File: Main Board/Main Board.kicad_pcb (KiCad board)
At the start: 4 copper layers, 100 x 62.5 mm, 104 parts, among them IC1 ESP32-S3-WROOM-1-N8R2, IC2 TPS65185RSLT, IC4 AP61100, J2 5023520300, J3 FH26W-39S-0.3SHW(60), J4 5023520500, J5 MSD-1-A, J6 5023520200, Q1 2N7002, Q2 BSS84-7-F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

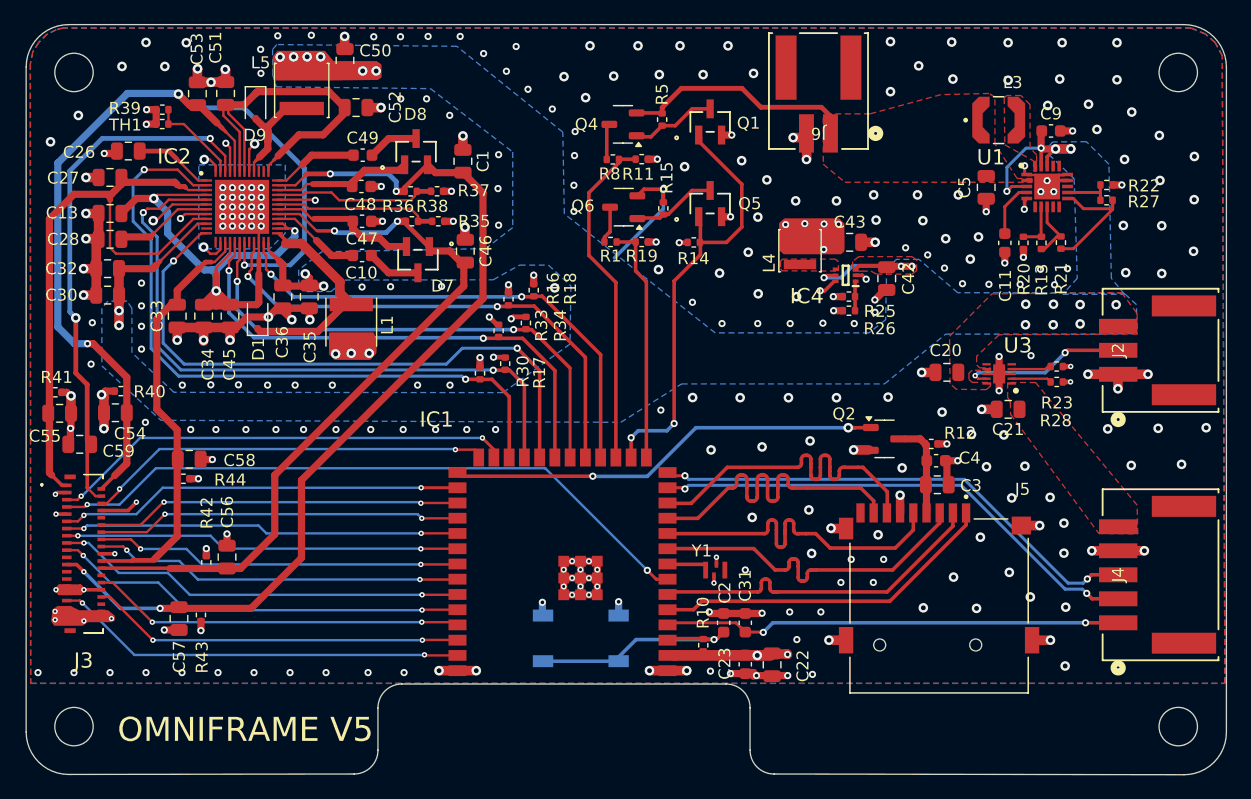
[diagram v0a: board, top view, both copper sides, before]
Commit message: fix silkscreen
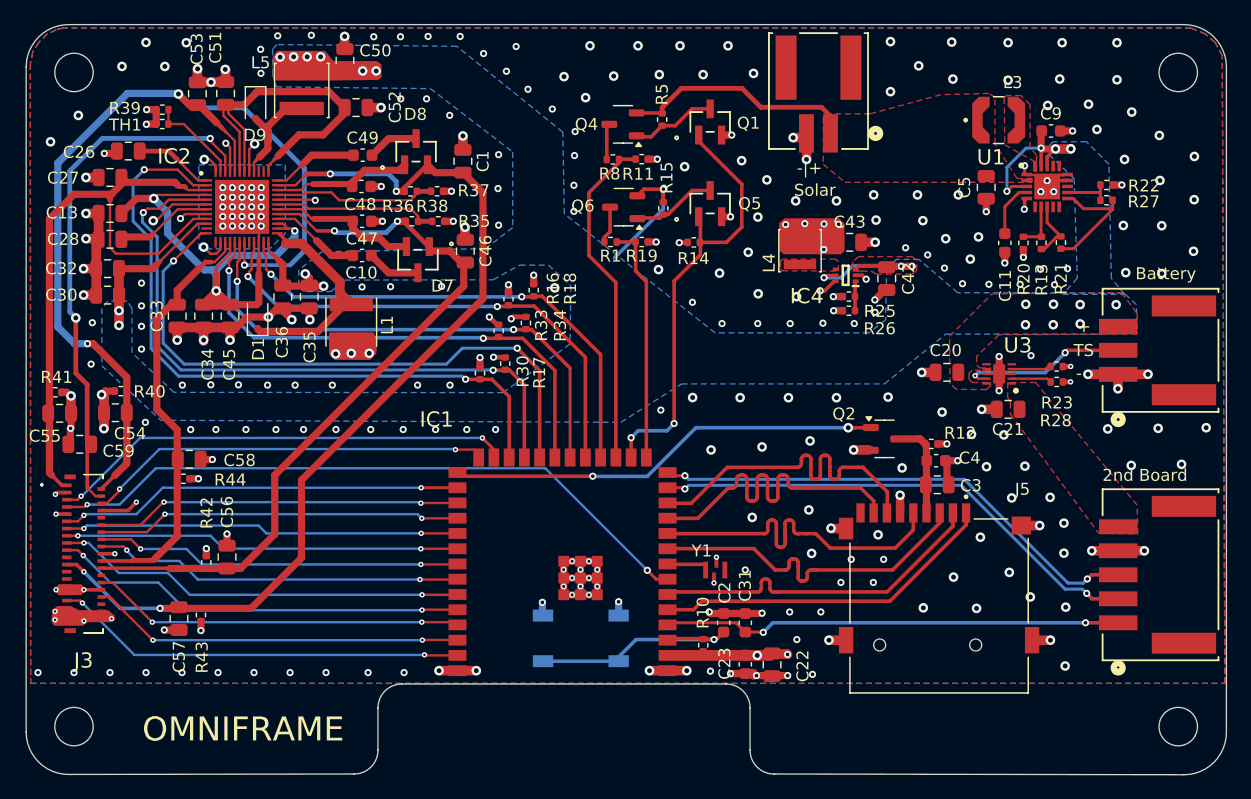
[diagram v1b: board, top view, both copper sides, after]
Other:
- board text added: "+"
- board text added: "-"
- board text added: "-|+"
- board text added: "2nd Board"
- board text added: "Battery"
- board text added: "OMNIFRAME"
- board text added: "Solar"
- board text added: "TS"
- board text removed: "OMNIFRAME V5"
